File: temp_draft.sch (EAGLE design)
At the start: 22 parts, among them IC1 NCS21911SN2T1G, IC2 NCS21911SN2T1G, IC3 NCS21911SN2T1G, IC4 NCS21911SN2T1G

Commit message: saved
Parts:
- removed JP1: (no value), pinhead:PINHD-1X5
- added R11: PTS120601B1K00P100, SamacSys_Parts:PTS120601B1K00P100
- added R12: ERA-6ARW563V, SamacSys_Parts:ERA-6ARW563V
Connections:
- removed net OUTPU1: JP1.2
- new net N$4: R11.2
- net GND: no longer JP1.5
- net INPUT1: now also R11.1, R12.2; no longer JP1.1
- net OUTPUT2: no longer JP1.3
- net OUTPUT3: no longer JP1.4
- net V: now also R12.1
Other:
- moved on the sheet: C1, C2, C3, C4, C5, C6, C7, IC1, IC2, IC3, IC4, JP2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

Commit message: rev_2 ready for layout, sch part incomplete info
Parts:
- added C10, C11, C8, C9: CGA3E2X7R1H104K080AE, SamacSys_Parts:CGA3E2X7R1H104K080AE
- added TP1, TP2, TP3, TP4, TP5, TP6, TP7, TP8: (no value), SamacSys_Parts:S1751-46R
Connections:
- removed net N$4: R11.2
- removed net V: JP2.1, R12.1
- new net V_12V: C10.1, C11.1, C8.1, C9.1, IC1.VDD, IC2.VDD, IC3.VDD, IC4.VDD, JP2.1, R12.1
- net GND: now also C10.2, C11.2, C8.2, C9.2, IC1.VSS, IC2.VSS, IC3.VSS, IC4.VSS, R11.2, TP5.TP, TP6.TP, TP7.TP, TP8.TP
- net INPUT1: now also TP1.TP
- net OUTPUT1: now also TP2.TP
- net OUTPUT2: now also TP3.TP
- net OUTPUT3: now also TP4.TP
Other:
- moved on the sheet: C1, C2, C3, C4, C5, C6, C7, IC1, IC2, IC3, IC4, R1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

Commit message: base board layout, done
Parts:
- added TP10, TP9: (no value), SamacSys_Parts:S1751-46R
- JP2: device pinhead:PINHD-1X6/90 -> pinhead:PINHD-1X7
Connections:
- removed net N$8: C2.1, R7.2
- new net OUTPUT4: C2.1, JP2.6, R7.2, TP9.TP
- net GND: now also JP2.7, TP10.TP; no longer JP2.6
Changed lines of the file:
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@@
 <part name="R4" library="SamacSys_Parts" deviceset="ERA-6AEB9091V" device=""/>
 <part name="R10" library="SamacSys_Parts" deviceset="RN73H2ATTD1043B25" device=""/>
-<part name="JP2" library="pinhead" library_urn="urn:adsk.eagle:library:325" deviceset="PINHD-1X6" device="/90" package3d_urn="urn:adsk.eagle:package:22475/2"/>
 <part name="R11" library="SamacSys_Parts" deviceset="PTS120601B1K00P100" device=""/>
 <part name="R12" library="SamacSys_Parts" deviceset="ERA-6ARW563V" device=""/>
@@
 <part name="C10" library="SamacSys_Parts" deviceset="CGA3E2X7R1H104K080AE" device=""/>
 <part name="C11" library="SamacSys_Parts" deviceset="CGA3E2X7R1H104K080AE" device=""/>
+<part name="TP9" library="SamacSys_Parts" deviceset="S1751-46R" device=""/>
+<part name="TP10" library="SamacSys_Parts" deviceset="S1751-46R" device=""/>
+<part name="JP2" library="pinhead" library_urn="urn:adsk.eagle:library:325" deviceset="PINHD-1X7" device="" package3d_urn="urn:adsk.eagle:package:22477/2"/>
 </parts>
 <sheets>
@@
 <attribute name="VALUE" x="204.47" y="26.67" size="1.778" layer="96" align="center-left"/>
 </instance>
-<instance part="JP2" gate="A" x="20.32" y="43.18" smashed="yes">
-<attribute name="NAME" x="13.97" y="53.975" size="1.778" layer="95"/>
-<attribute name="VALUE" x="13.97" y="33.02" size="1.778" layer="96"/>
-</instance>
 <instance part="R11" gate="G$1" x="78.74" y="50.8" smashed="yes" rot="R270">
 <attribute name="NAME" x="85.09" y="49.53" size="1.778" layer="95" rot="R270" align="center-left"/>
@@
 <attribute name="NAME" x="417.83" y="3.81" size="1.778" layer="95" rot="R270" align="center-left"/>
 <attribute name="VALUE" x="415.29" y="3.81" size="1.778" layer="96" rot="R270" align="center-left"/>
+</instance>
+<instance part="TP9" gate="G$1" x="-22.86" y="-15.24" smashed="yes">
+<attribute name="VALUE" x="-27.94" y="-20.32" size="1.27" layer="96"/>
+<attribute name="NAME" x="-27.94" y="-22.86" size="1.27" layer="95"/>
+</instance>
+<instance part="TP10" gate="G$1" x="-2.54" y="-15.24" smashed="yes">
+<attribute name="VALUE" x="-7.62" y="-20.32" size="1.27" layer="96"/>
+<attribute name="NAME" x="-7.62" y="-22.86" size="1.27" layer="95"/>
+</instance>
+<instance part="JP2" gate="A" x="33.02" y="20.32" smashed="yes" rot="MR0">
+<attribute name="NAME" x="39.37" y="31.115" size="1.778" layer="95" rot="MR0"/>
+<attribute name="VALUE" x="39.37" y="7.62" size="1.778" layer="96" rot="MR0"/>
 </instance>
 </instances>
@@
 </segment>
 <segment>
-<pinref part="JP2" gate="A" pin="2"/>
-<wire x1="17.78" y1="48.26" x2="22.86" y2="48.26" width="0.1524" layer="91"/>
-<label x="25.4" y="48.26" size="1.778" layer="95"/>
-</segment>
-<segment>
 <wire x1="76.2" y1="53.34" x2="78.74" y2="53.34" width="0.1524" layer="91"/>
 <wire x1="78.74" y1="53.34" x2="78.74" y2="50.8" width="0.1524" layer="91"/>
@@
 <label x="-20.32" y="63.5" size="1.778" layer="95"/>
 </segment>
+<segment>
+<pinref part="JP2" gate="A" pin="2"/>
+<wire x1="35.56" y1="25.4" x2="40.64" y2="25.4" width="0.1524" layer="91"/>
+<label x="43.18" y="25.4" size="1.778" layer="95"/>
+</segment>
 </net>
 <net name="GND" class="0">
@@
 </segment>
 <segment>
-<pinref part="JP2" gate="A" pin="6"/>
-<wire x1="17.78" y1="38.1" x2="22.86" y2="38.1" width="0.1524" layer="91"/>
-<label x="25.4" y="38.1" size="1.778" layer="95"/>
-</segment>
-<segment>
 <pinref part="R11" gate="G$1" pin="2"/>
 <wire x1="78.74" y1="33.02" x2="78.74" y2="30.48" width="0.1524" layer="91"/>
@@
 <wire x1="411.48" y1="0" x2="411.48" y2="-2.54" width="0.1524" layer="91"/>
 <label x="408.94" y="-2.54" size="1.778" layer="95" rot="R90"/>
+</segment>
+<segment>
+<pinref part="TP10" gate="G$1" pin="TP"/>
+<wire x1="-2.54" y1="-7.62" x2="-2.54" y2="-5.08" width="0.1524" layer="91"/>
+<label x="0" y="-5.08" size="1.778" layer="95"/>
+</segment>
+<segment>
+<pinref part="JP2" gate="A" pin="7"/>
+<wire x1="35.56" y1="12.7" x2="40.64" y2="12.7" width="0.1524" layer="91"/>
+<label x="43.18" y="12.7" size="1.778" layer="95"/>
 </segment>
 </net>
@@
 </segment>
 <segment>
-<pinref part="JP2" gate="A" pin="3"/>
-<wire x1="17.78" y1="45.72" x2="22.86" y2="45.72" width="0.1524" layer="91"/>
-<label x="25.4" y="45.72" size="1.778" layer="95"/>
-</segment>
-<segment>
 <pinref part="TP2" gate="G$1" pin="TP"/>
 <wire x1="-22.86" y1="45.72" x2="-22.86" y2="48.26" width="0.1524" layer="91"/>
 <label x="-20.32" y="48.26" size="1.778" layer="95"/>
+</segment>
+<segment>
+<pinref part="JP2" gate="A" pin="3"/>
+<wire x1="35.56" y1="22.86" x2="40.64" y2="22.86" width="0.1524" layer="91"/>
+<label x="43.18" y="22.86" size="1.778" layer="95"/>
 </segment>
 </net>
@@
 </segment>
 <segment>
-<pinref part="JP2" gate="A" pin="4"/>
-<wire x1="17.78" y1="43.18" x2="22.86" y2="43.18" width="0.1524" layer="91"/>
-<label x="25.4" y="43.18" size="1.778" layer="95"/>
-</segment>
-<segment>
 <pinref part="TP3" gate="G$1" pin="TP"/>
 <wire x1="-22.86" y1="30.48" x2="-22.86" y2="33.02" width="0.1524" layer="91"/>
 <label x="-20.32" y="33.02" size="1.778" layer="95"/>
+</segment>
+<segment>
+<pinref part="JP2" gate="A" pin="4"/>
+<wire x1="35.56" y1="20.32" x2="40.64" y2="20.32" width="0.1524" layer="91"/>
+<label x="43.18" y="20.32" size="1.778" layer="95"/>
 </segment>
 </net>
@@
 </segment>
 <segment>
-<pinref part="JP2" gate="A" pin="5"/>
-<wire x1="17.78" y1="40.64" x2="22.86" y2="40.64" width="0.1524" layer="91"/>
-<label x="25.4" y="40.64" size="1.778" layer="95"/>
-</segment>
-<segment>
 <pinref part="TP4" gate="G$1" pin="TP"/>
 <wire x1="-22.86" y1="12.7" x2="-22.86" y2="15.24" width="0.1524" layer="91"/>
 <label x="-20.32" y="15.24" size="1.778" layer="95"/>
+</segment>
+<segment>
+<pinref part="JP2" gate="A" pin="5"/>
+<wire x1="35.56" y1="17.78" x2="40.64" y2="17.78" width="0.1524" layer="91"/>
+<label x="43.18" y="17.78" size="1.778" layer="95"/>
 </segment>
 </net>
@@
 </segment>
 </net>
-<net name="N$8" class="0">
+<net name="OUTPUT4" class="0">
 <segment>
 <pinref part="R7" gate="G$1" pin="2"/>
@@
 <wire x1="365.76" y1="40.64" x2="368.3" y2="40.64" width="0.1524" layer="91"/>
 <pinref part="C2" gate="G$1" pin="1"/>
+<label x="365.76" y="48.26" size="1.778" layer="95"/>
+</segment>
+<segment>
+<pinref part="TP9" gate="G$1" pin="TP"/>
+<wire x1="-22.86" y1="-7.62" x2="-22.86" y2="-5.08" width="0.1524" layer="91"/>
+<label x="-20.32" y="-5.08" size="1.778" layer="95"/>
+</segment>
+<segment>
+<pinref part="JP2" gate="A" pin="6"/>
+<wire x1="35.56" y1="15.24" x2="40.64" y2="15.24" width="0.1524" layer="91"/>
+<label x="43.18" y="15.24" size="1.778" layer="95"/>
 </segment>
 </net>
 <net name="V_12V" class="0">
-<segment>
-<pinref part="JP2" gate="A" pin="1"/>
-<wire x1="17.78" y1="50.8" x2="22.86" y2="50.8" width="0.1524" layer="91"/>
-<label x="25.4" y="50.8" size="1.778" layer="95"/>
-</segment>
 <segment>
 <pinref part="IC1" gate="G$1" pin="VDD"/>
@@
 <pinref part="R12" gate="G$1" pin="1"/>
 </segment>
-</net>
+<segment>
+<pinref part="JP2" gate="A" pin="1"/>
+<wire x1="35.56" y1="27.94" x2="40.64" y2="27.94" width="0.1524" layer="91"/>
+<label x="43.18" y="27.94" size="1.778" layer="95"/>
+</segment>
+</net>

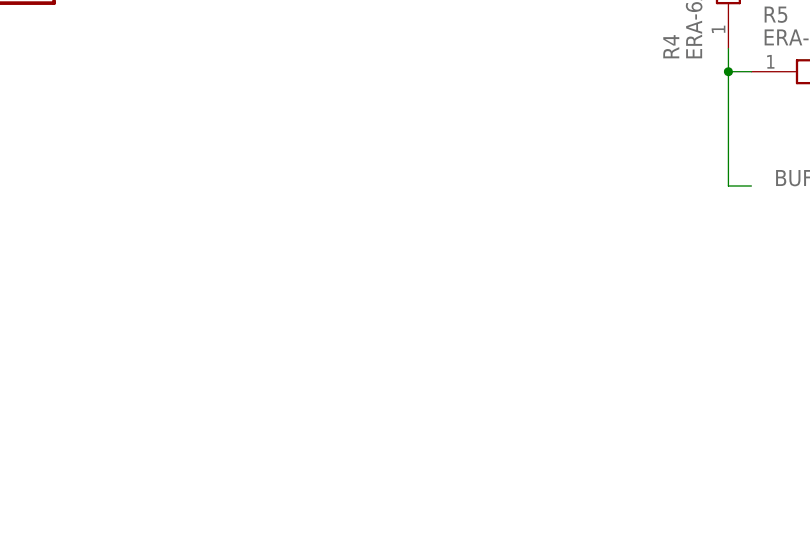
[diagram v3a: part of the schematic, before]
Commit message: with LED and tented Vias
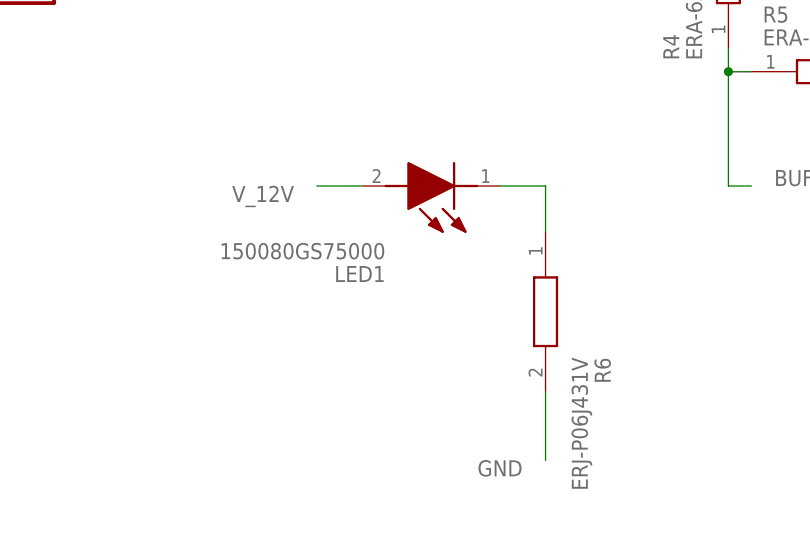
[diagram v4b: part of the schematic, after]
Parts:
- added LED1: 150080GS75000, SamacSys_Parts:150080GS75000
- added R6: ERJ-P06J431V, SamacSys_Parts:ERJ-P06J431V
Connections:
- new net N$20: LED1.K, R6.1
- net GND: now also R6.2
- net V_12V: now also LED1.A
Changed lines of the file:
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@@
 <part name="TP10" library="SamacSys_Parts" deviceset="S1751-46R" device=""/>
 <part name="JP2" library="pinhead" library_urn="urn:adsk.eagle:library:325" deviceset="PINHD-1X7" device="" package3d_urn="urn:adsk.eagle:package:22477/2"/>
+<part name="LED1" library="SamacSys_Parts" deviceset="150080GS75000" device=""/>
+<part name="R6" library="SamacSys_Parts" deviceset="ERJ-P06J431V" device=""/>
 </parts>
 <sheets>
@@
 <attribute name="VALUE" x="39.37" y="7.62" size="1.778" layer="96" rot="MR0"/>
 </instance>
+<instance part="LED1" gate="G$1" x="88.9" y="-10.16" smashed="yes" rot="R180">
+<attribute name="NAME" x="76.2" y="-19.05" size="1.778" layer="95" rot="R180"/>
+<attribute name="VALUE" x="76.2" y="-16.51" size="1.778" layer="96" rot="R180"/>
+</instance>
+<instance part="R6" gate="G$1" x="93.98" y="-15.24" smashed="yes" rot="R270">
+<attribute name="NAME" x="100.33" y="-29.21" size="1.778" layer="95" rot="R270" align="center-left"/>
+<attribute name="VALUE" x="97.79" y="-29.21" size="1.778" layer="96" rot="R270" align="center-left"/>
+</instance>
 </instances>
 <busses>
@@
 <wire x1="35.56" y1="12.7" x2="40.64" y2="12.7" width="0.1524" layer="91"/>
 <label x="43.18" y="12.7" size="1.778" layer="95"/>
+</segment>
+<segment>
+<pinref part="R6" gate="G$1" pin="2"/>
+<wire x1="93.98" y1="-33.02" x2="93.98" y2="-40.64" width="0.1524" layer="91"/>
+<label x="91.44" y="-40.64" size="1.778" layer="95" rot="R180"/>
 </segment>
 </net>
@@
 <label x="43.18" y="27.94" size="1.778" layer="95"/>
 </segment>
-</net>
+<segment>
+<pinref part="LED1" gate="G$1" pin="A"/>
+<wire x1="73.66" y1="-10.16" x2="68.58" y2="-10.16" width="0.1524" layer="91"/>
+<label x="66.04" y="-10.16" size="1.778" layer="95" rot="R180"/>
+</segment>
+</net>
+<net name="N$20" class="0">
+<segment>
+<pinref part="LED1" gate="G$1" pin="K"/>
+<wire x1="88.9" y1="-10.16" x2="93.98" y2="-10.16" width="0.1524" layer="91"/>
+<wire x1="93.98" y1="-10.16" x2="93.98" y2="-15.24" width="0.1524" layer="91"/>
+<pinref part="R6" gate="G$1" pin="1"/>
+</segment>
+</net>
